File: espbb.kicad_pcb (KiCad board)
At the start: 2 copper layers, 20 x 20 mm, 10 parts, among them P1 CONN_8, P2 CONN_8, SW1 SWITCH_INV, U1 ESP-12/07v2/08v2, U2 LM6206

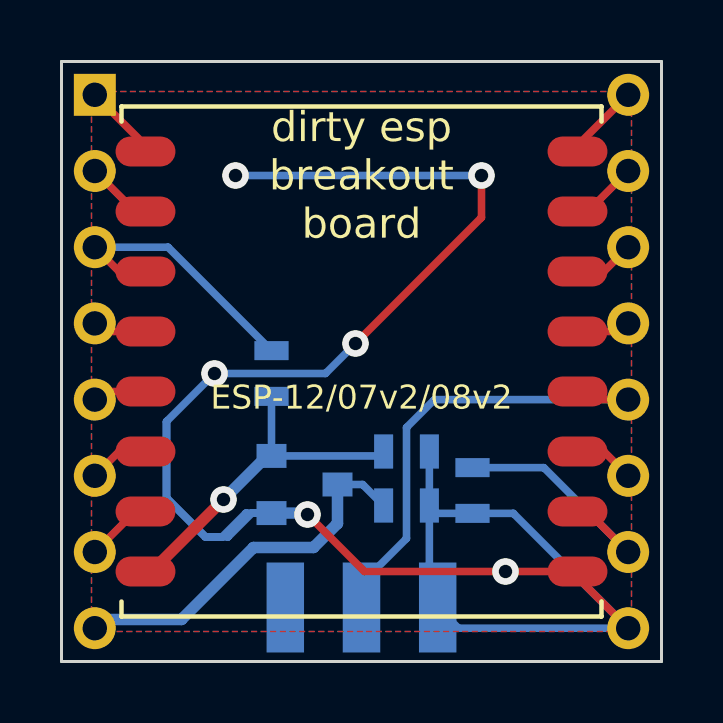
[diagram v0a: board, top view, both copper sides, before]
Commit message: fix DRC warnings
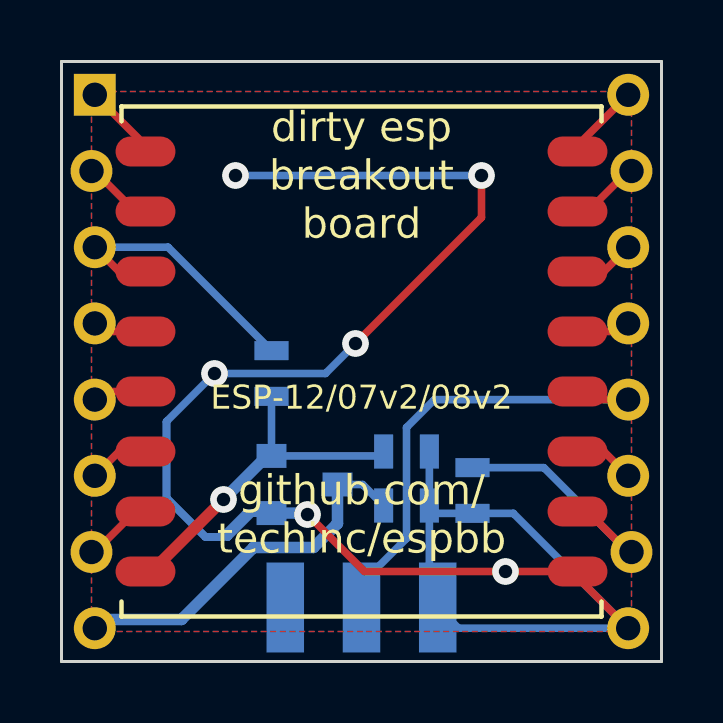
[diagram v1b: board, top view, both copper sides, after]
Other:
- board text added: "github.com/ techinc/espbb"
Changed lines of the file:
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@@
     (area -10.131829 -10.131829 10.050001 12.02397)
     (thickness 1.6)
-    (drawings 21)
+    (drawings 22)
     (tracks 94)
     (zones 0)
@@
     (mod_text_size 1 1)
     (mod_text_width 0.15)
-    (pad_size 1.25 3)
-    (pad_drill 0)
+    (pad_size 1.397 1.397)
+    (pad_drill 0.8128)
     (pad_to_mask_clearance 0)
     (aux_axis_origin 0 0)
@@
       (net 10 N-0000018)
     )
-    (pad 2 thru_hole circle (at -6.35 0 270) (size 1.397 1.397) (drill 0.8128)
+    (pad 2 thru_hole circle (at -6.35 0.11 270) (size 1.397 1.397) (drill 0.8128)
       (layers *.Cu *.Mask F.SilkS)
       (net 9 N-0000017)
@@
       (net 5 N-0000013)
     )
-    (pad 7 thru_hole circle (at 6.35 0 270) (size 1.397 1.397) (drill 0.8128)
+    (pad 7 thru_hole circle (at 6.35 0.11 270) (size 1.397 1.397) (drill 0.8128)
       (layers *.Cu *.Mask F.SilkS)
       (net 4 N-0000012)
@@
       (zone_connect 2)
     )
-    (pad 2 thru_hole circle (at -6.35 0 90) (size 1.397 1.397) (drill 0.8128)
+    (pad 2 thru_hole circle (at -6.35 0.11 90) (size 1.397 1.397) (drill 0.8128)
       (layers *.Cu *.Mask F.SilkS)
       (net 16 N-000009)
@@
       (net 12 N-000005)
     )
-    (pad 7 thru_hole circle (at 6.35 0 90) (size 1.397 1.397) (drill 0.8128)
+    (pad 7 thru_hole circle (at 6.35 0.11 90) (size 1.397 1.397) (drill 0.8128)
       (layers *.Cu *.Mask F.SilkS)
       (net 11 N-000004)
@@
       (xy -2.49428 -0.762) (xy -2.51714 -0.66548)) (layer B.SilkS) (width 0.00254))
   )
+  (gr_text "github.com/\ntechinc/espbb" (at 0 5.1) (layer F.SilkS)
+    (effects (font (size 1 1) (thickness 0.1)))
+  )
   (gr_text "dirty esp\nbreakout\nboard" (at 0 -6.2) (layer F.SilkS)

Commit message: change gpio number
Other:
- board text added: "GPIO2"
- board text removed: "GPIO1"
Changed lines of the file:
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@@
     (effects (font (size 0.8 0.8) (thickness 0.1)) (justify mirror))
   )
-  (gr_text GPIO1 (at 6.096 3.81) (layer B.SilkS)
+  (gr_text GPIO2 (at 6.096 3.81) (layer B.SilkS)
     (effects (font (size 0.8 0.8) (thickness 0.1)) (justify mirror))
   )
